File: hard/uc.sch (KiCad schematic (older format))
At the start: 6 parts, among them J1 Conn_01x06

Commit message: attribute naming update
JLCPCB_Part_Number -> LCSC
DigiKey_Part_Number -> DigiKey
Mouser_Part_Number -> Mouser
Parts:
- MCU1: DigiKey (none) -> 497-15375-ND; DigiKey_Part_Number 497-15375-ND -> (none); JLCPCB_Part_Number C91929 -> (none); LCSC (none) -> C91929
- MCU1: JLCPCB_Part_Number C91929 -> (none); LCSC (none) -> C91929
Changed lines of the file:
@@
 F 2 "led_matrix:LQFP-100_14x14mm_P0.5mm" H 5800 2700 50  0001 C CNN
 F 3 "https://www.st.com/resource/en/datasheet/stm32f446ve.pdf" H 5800 2700 50  0001 C CNN
-F 4 "C91929" H 5250 2350 50  0001 C CNN "JLCPCB_Part_Number"
+F 4 "C91929" H 5250 2350 50  0001 C CNN "LCSC"
 F 5 "STMicroelectronics" H 5250 2350 50  0001 C CNN "MF"
 F 6 "STM32F446VET6" H 5250 2350 50  0001 C CNN "MPN"
@@
 F 2 "led_matrix:LQFP-100_14x14mm_P0.5mm" H 4100 6150 50  0001 C CNN
 F 3 "https://www.st.com/resource/en/datasheet/stm32f446ve.pdf" H 4100 6150 50  0001 C CNN
-F 4 "C91929" H 3550 5800 50  0001 C CNN "JLCPCB_Part_Number"
+F 4 "C91929" H 3550 5800 50  0001 C CNN "LCSC"
 F 5 "STMicroelectronics" H 3550 5800 50  0001 C CNN "MF"
 F 6 "STM32F446VET6" H 3550 5800 50  0001 C CNN "MPN"
@@
 F 2 "led_matrix:LQFP-100_14x14mm_P0.5mm" H 5500 1550 50  0001 C CNN
 F 3 "https://www.st.com/resource/en/datasheet/stm32f446ve.pdf" H 5500 1550 50  0001 C CNN
-F 4 "C91929" H 4950 1200 50  0001 C CNN "JLCPCB_Part_Number"
+F 4 "C91929" H 4950 1200 50  0001 C CNN "LCSC"
 F 5 "STMicroelectronics" H 4950 1200 50  0001 C CNN "MF"
 F 6 "STM32F446VET6" H 4950 1200 50  0001 C CNN "MPN"
 F 7 "ST MICROELECTRONICS LQFP-100_14X14X05P ROHS" H 4950 1200 50  0001 C CNN "Description"
-F 8 "497-15375-ND" H 4950 1200 50  0001 C CNN "DigiKey_Part_Number"
+F 8 "497-15375-ND" H 4950 1200 50  0001 C CNN "DigiKey"
 	1    4950 1200
 	1    0    0    -1
@@
 F 2 "led_matrix:LQFP-100_14x14mm_P0.5mm" H 4950 5000 50  0001 C CNN
 F 3 "https://www.st.com/resource/en/datasheet/stm32f446ve.pdf" H 4950 5000 50  0001 C CNN
-F 4 "C91929" H 4400 4650 50  0001 C CNN "JLCPCB_Part_Number"
+F 4 "C91929" H 4400 4650 50  0001 C CNN "LCSC"
 F 5 "STMicroelectronics" H 4400 4650 50  0001 C CNN "MF"
 F 6 "STM32F446VET6" H 4400 4650 50  0001 C CNN "MPN"
 F 7 "ST MICROELECTRONICS LQFP-100_14X14X05P ROHS" H 4400 4650 50  0001 C CNN "Description"
-F 8 "497-15375-ND" H 4400 4650 50  0001 C CNN "DigiKey_Part_Number"
+F 8 "497-15375-ND" H 4400 4650 50  0001 C CNN "DigiKey"
 	4    4400 4650
 	1    0    0    -1
@@
 F 2 "led_matrix:LQFP-100_14x14mm_P0.5mm" H 5900 3850 50  0001 C CNN
 F 3 "https://www.st.com/resource/en/datasheet/stm32f446ve.pdf" H 5900 3850 50  0001 C CNN
-F 4 "C91929" H 5350 3500 50  0001 C CNN "JLCPCB_Part_Number"
+F 4 "C91929" H 5350 3500 50  0001 C CNN "LCSC"
 F 5 "STMicroelectronics" H 5350 3500 50  0001 C CNN "MF"
 F 6 "STM32F446VET6" H 5350 3500 50  0001 C CNN "MPN"

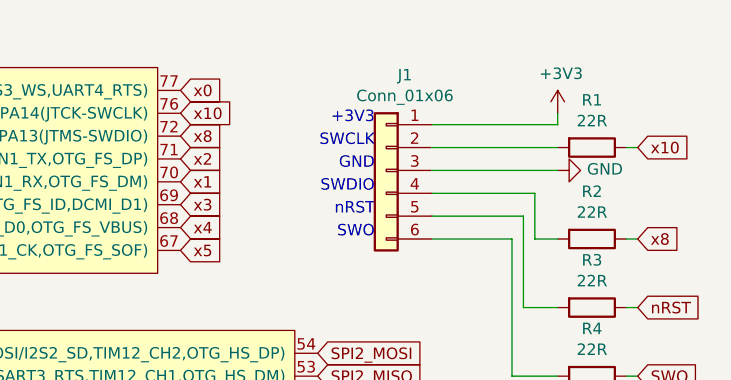
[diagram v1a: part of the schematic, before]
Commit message: added lcsc number for debug header
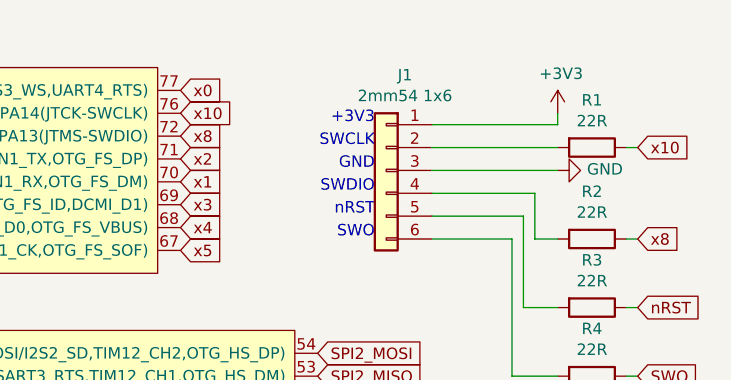
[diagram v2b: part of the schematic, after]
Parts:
- J1: value Conn_01x06 -> 2mm54 1x6; LCSC (none) -> C492414
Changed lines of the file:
@@
 P 9600 1650
 F 0 "J1" H 9518 2067 50  0000 C CNN
-F 1 "Conn_01x06" H 9518 1976 50  0000 C CNN
+F 1 "2mm54 1x6" H 9518 1976 50  0000 C CNN
 F 2 "Connector_PinHeader_2.54mm:PinHeader_1x06_P2.54mm_Horizontal" H 9600 1650 50  0001 C CNN
 F 3 "~" H 9600 1650 50  0001 C CNN
+F 4 "C492414" H 9600 1650 50  0001 C CNN "LCSC"
 	1    9600 1650
 	-1   0    0    -1
